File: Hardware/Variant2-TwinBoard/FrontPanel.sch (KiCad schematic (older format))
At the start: 18 parts, among them J11 Power_Conn, J7 Control_Conn, SW1 SW_Push, SW2 SW_Push, SW3 SW_Push, SW4 SW_Push, SW5 SW_Push, SW6 SW_Push, U6 TCA9534

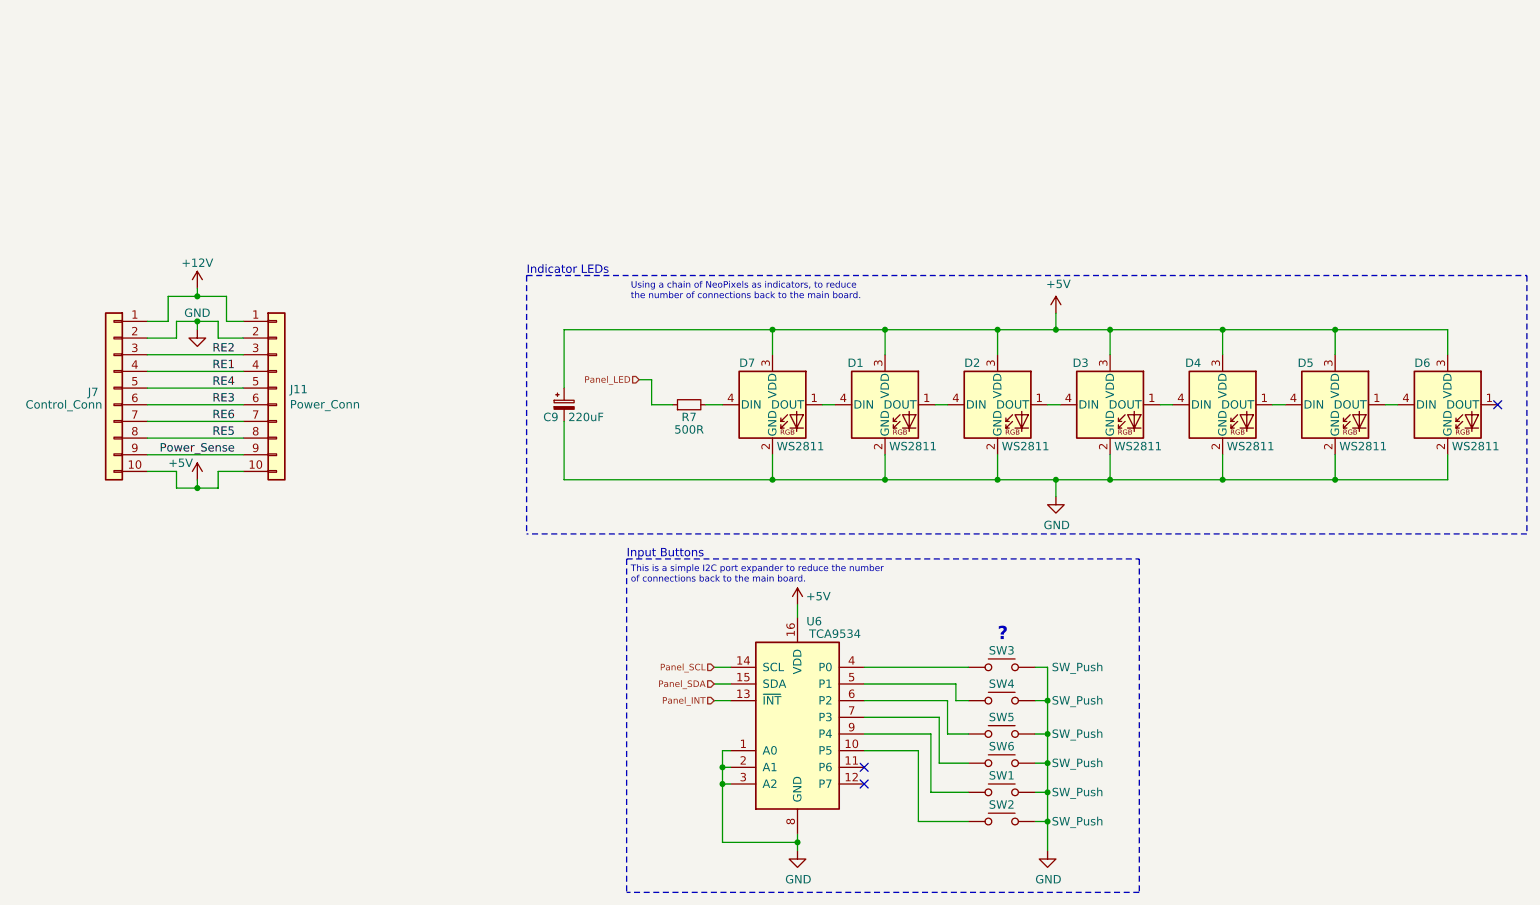
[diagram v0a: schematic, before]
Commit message: New TwinBoard layout
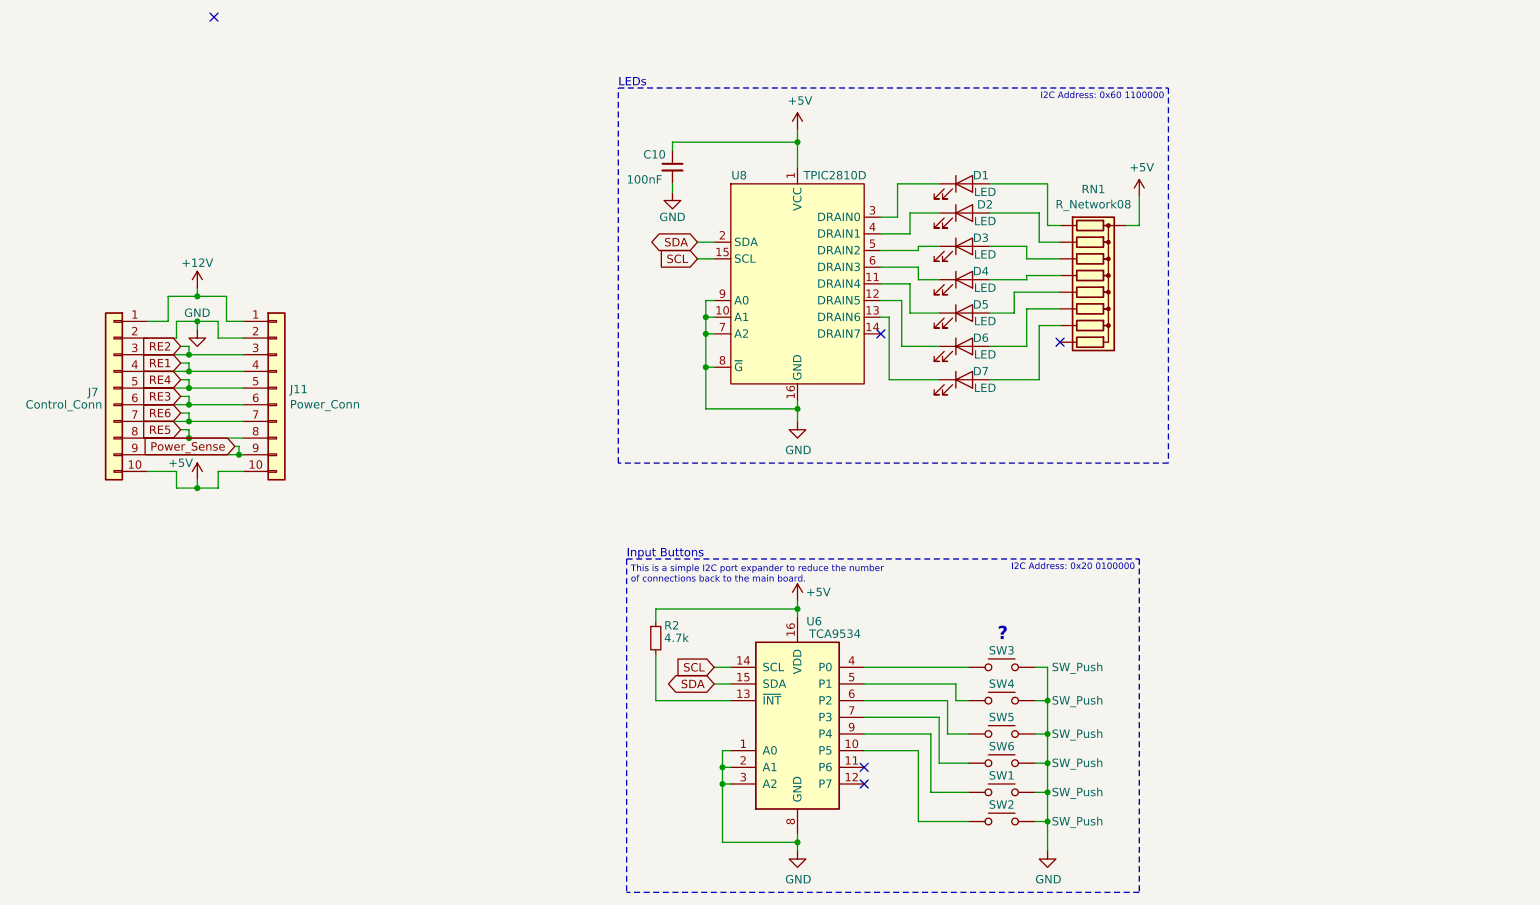
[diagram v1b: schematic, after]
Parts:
- removed C9: 220uF, Capacitor_SMD:CP_Elec_8x6.2, symbol AquaHub-rescue:CP_Small-Device
- removed D1, D2, D3, D4, D5, D6, D7: WS2811, LED_THT:LED_D5.0mm-4_RGB, symbol AquaHub-rescue:NeoPixel_THT-LED
- removed R7: 500R, Resistor_SMD:R_0603_1608Metric_Pad1.05x0.95mm_HandSolder, symbol AquaHub-rescue:R_Small-Device
- added C10: 100nF, Capacitor_SMD:C_0603_1608Metric_Pad1.05x0.95mm_HandSolder, symbol Device:C_Small
- added D1, D2, D3, D4, D5, D6, D7: LED, LED_THT:LED_D5.0mm, symbol Device:LED
- added R2: 4.7k, Resistor_SMD:R_0603_1608Metric_Pad1.05x0.95mm_HandSolder, symbol Device:R_Small
- added RN1: R_Network08, AquaFootprints:CAT25, symbol Device:R_Network08
- added U8: TPIC2810D, Package_SO:SOIC-16_3.9x9.9mm_P1.27mm, symbol Driver_LED:TPIC2810D
- J11, SW1, SW2, SW3, SW4, SW5, SW6, U6: Vendor (none) -> Mouser
- J7: footprint Connector_PinHeader_2.54mm:PinHeader_2x05_P2.54mm_Vertical -> Connector_IDC:IDC-Header_2x05_P2.54mm_Vertical
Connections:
- net +5V: now also C10.1, R2.1, RN1.1 (common), U8.1 (VCC)
- net GND: now also C10.2, U8.10 (A1), U8.16 (GND), U8.7 (A2), U8.8 (~G), U8.9 (A0)
- net Panel_INT: no longer names the net of U6.13 (~INT~)
- net Panel_INT: now also R2.2
- net Panel_SCL renamed SCL
- net SCL: now also U8.15 (SCL)
- net Panel_SDA renamed SDA
- net SDA: now also U8.2 (SDA)
- new net: D1.1 (K), U8.3 (DRAIN0)
- new net: D1.2 (A), RN1.2 (R1)
- new net: D2.1 (K), U8.4 (DRAIN1)
- new net: D2.2 (A), RN1.3 (R2)
- new net: D3.1 (K), U8.5 (DRAIN2)
- new net: D3.2 (A), RN1.4 (R3)
- new net: D4.1 (K), U8.6 (DRAIN3)
- new net: D4.2 (A), RN1.5 (R4)
- new net: D5.1 (K), U8.11 (DRAIN4)
- new net: D5.2 (A), RN1.6 (R5)
- new net: D6.1 (K), U8.12 (DRAIN5)
- new net: D6.2 (A), RN1.7 (R6)
- new net: D7.1 (K), U8.13 (DRAIN6)
- new net: D7.2 (A), RN1.8 (R7)
- no-connect marks 3 -> 5
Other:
- note added: "I2C Address: 0x20 0100000"
- note added: "I2C Address: 0x60 1100000"
- note added: "LEDs"
- note removed: "Indicator LEDs"
- note removed: "Using a chain of NeoPixels as indicators, to reduce\nthe number of connections back to the main board."
